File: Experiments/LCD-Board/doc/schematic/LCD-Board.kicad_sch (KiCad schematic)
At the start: 7 parts, among them J1 Conn_01x04_Pin, SW1 RotaryEncoder_Switch, U1 ATmega328P-P, U2 LM16255K, Y1 Crystal

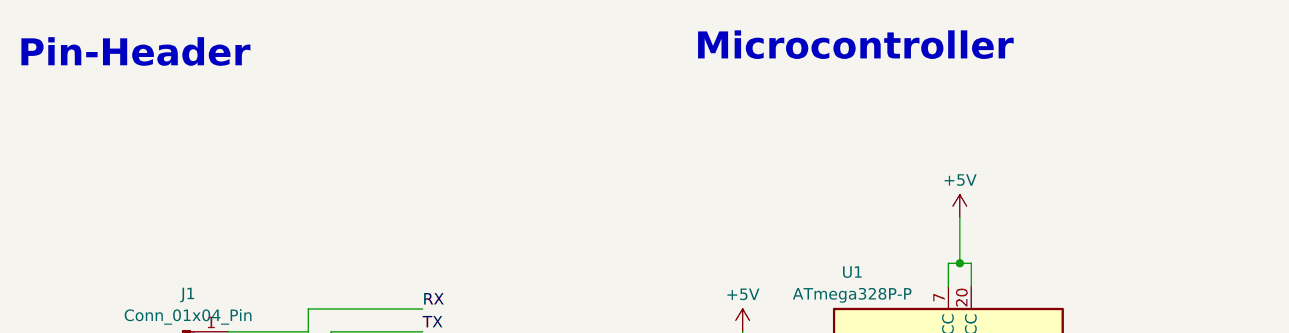
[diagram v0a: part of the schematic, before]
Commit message: LCD-Board: Typos in schematic
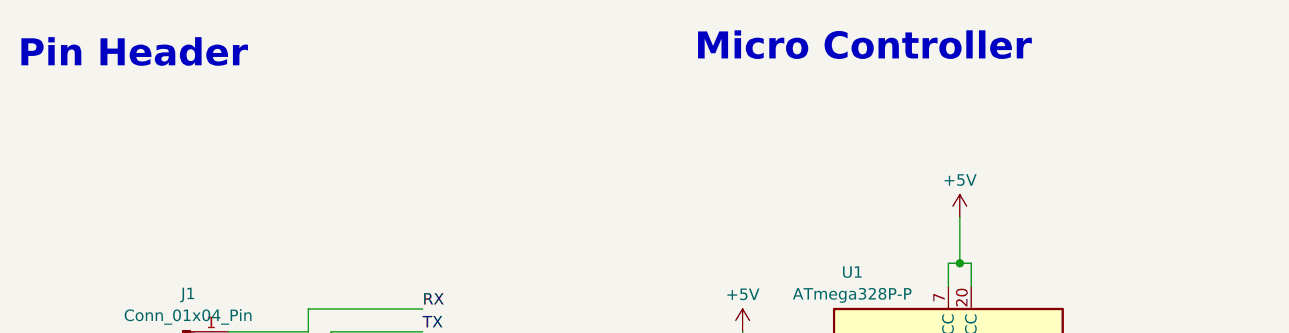
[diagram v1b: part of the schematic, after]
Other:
- note added: "Micro Controller"
- note added: "Pin Header"
- note removed: "Microcontroller"
- note removed: "Pin-Header"
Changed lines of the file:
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@@
 		(rev "1")
 		(company "Dennis Schulmeister-Zimolong")
-		(comment 2 "A Pin-Header providers power and a UART serial connection.")
-		(comment 3 "with an LC-Display, and a Switch / Rotary Encoder.")
-		(comment 4 "This is just a very basic Atmega328p MCU-Board")
+		(comment 2 "A pin header provides power and a UART serial connection.")
+		(comment 3 "with a 16x8 LCD and a switch / rotary encoder.")
+		(comment 4 "This is just a very basic Atmega328p MCU board")
 	)
-	(text "Pin-Header"
+	(text "Pin Header"
 		(exclude_from_sim no)
 		(at 26.162 38.608 0)
@@
 		)
 	)
-	(text "Microcontroller"
+	(text "Micro Controller"
 		(exclude_from_sim no)
 		(at 101.346 37.846 0)
